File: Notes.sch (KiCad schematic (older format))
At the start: 0 parts

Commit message: Some rearrangements/
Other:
- note added: "V1.6\n\nRework IC102"
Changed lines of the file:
@@
 encoding utf-8
 Sheet 6 6
-Title ""
-Date "2025-10-10"
-Rev "1.5"
-Comp ""
+Title "NANAO MS8-29 (05A00362G1)"
+Date "2025-11-17"
+Rev "1.6"
+Comp "Franck BOURDONNEC"
 Comment1 ""
 Comment2 ""
@@
 Text Notes 1050 2700 0    50   ~ 0
 V1.5\nupdate some values\nR303,R313,R323 from 62K to 220K\nR302,R312,R322 from 68 to 33\nR307,R317,R327 from 1/2W to 2W\n\n\nL570 : from 22µH to 100µH\n\nL301,L311,L321 : from 10µH to 22µH\n\nL302,L312,L322 : from 1µH to 1.8µH\n(not really really sure of ring colors\n brown,grey,gold\n red, violet, gold)\n\nfound 1K resistor on L301, named it R307\n\nSparkgap: 1Kv\n\nAdd D305, D315, D325 pcb-crt bodge\n\n\nC446 bipolar 33µ/16v
+Text Notes 3350 1000 0    50   ~ 0
+V1.6\n\nRework IC102
 $EndSCHEMATC

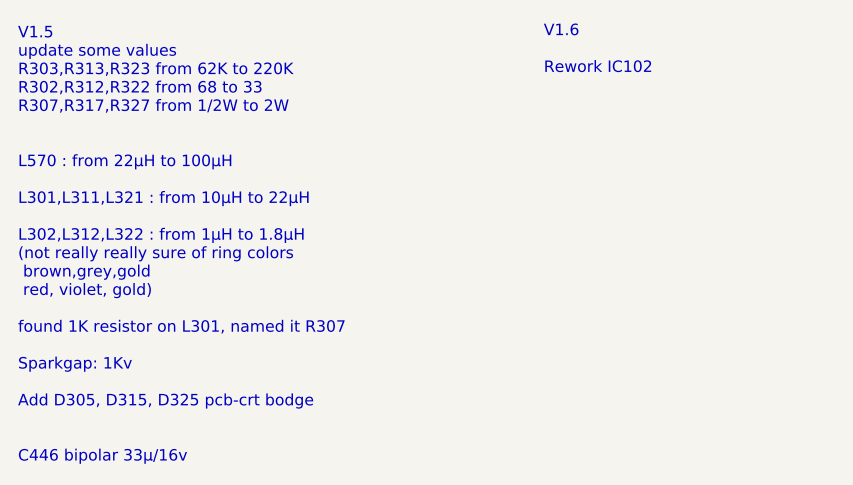
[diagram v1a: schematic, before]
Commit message: IC401 is LA7832 not LA7830
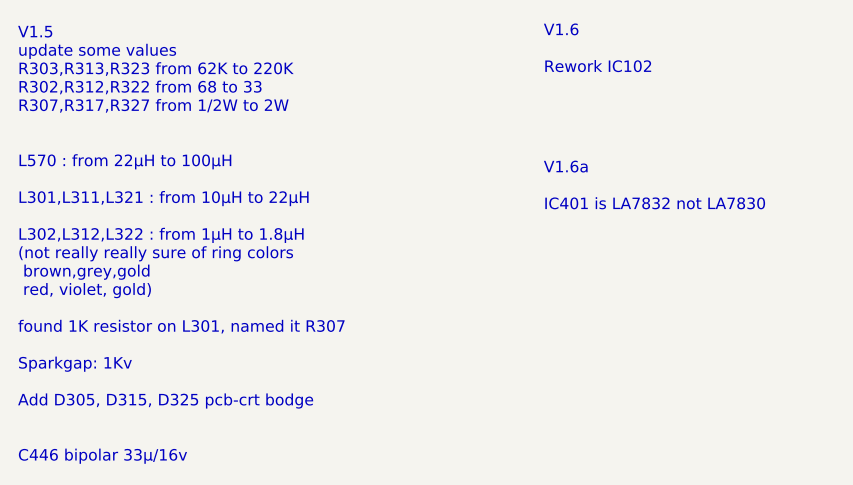
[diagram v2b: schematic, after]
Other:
- note added: "V1.6a\n\nIC401 is LA7832 not LA7830"
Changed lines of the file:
@@
 Sheet 6 6
 Title "NANAO MS8-29 (05A00362G1)"
-Date "2025-11-17"
-Rev "1.6"
+Date "2026-01-30"
+Rev "1.6a"
 Comp "Franck BOURDONNEC"
 Comment1 ""
@@
 Text Notes 3350 1000 0    50   ~ 0
 V1.6\n\nRework IC102
+Text Notes 3350 1600 0    50   ~ 0
+V1.6a\n\nIC401 is LA7832 not LA7830
 $EndSCHEMATC
